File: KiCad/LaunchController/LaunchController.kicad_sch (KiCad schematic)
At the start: 116 parts, among them J1 DC_IN, J10 CONN_SPEAKER, J11 CONN_EXT_I2C_0, J12 CONN_EXT_GPIO_0, J13 CONN_EXT_SPI_0, J14 CONN_EXT_I2C_1, J15 CONN_EXT_GPIO_1, J16 CONN_EXT_SPI_1, J17 CONN_USB, J18 CONN_EXT_I2C_2, J19 CONN_EXT_GPIO_2, J2 JMP_RUN, J20 CONN_EXT_SPI_2, J21 CONN_EXT_I2C_3, J22 CONN_EXT_GPIO_3, J3 CONN_ICSP, J4 CONN_RS485, J5 JMP_KILL, J6 CONN_AUDIO, J7 L, J8 R, J9 CONN_EXT_UART, P1 USB_C_Plug_USB2.0, Q1 TJ8S06M3L, Q2 TJ8S06M3L, Q3 2SC3325, SW1 SW_RESET, U1 SI-8008HFE, U3 INA219BxDCN, U4 INA219BxDCN, U5 74HC14, U6 LTC485CN8#PBF, U7 FT232RL, U8 ATmega2560-16A, Y1 16MHz

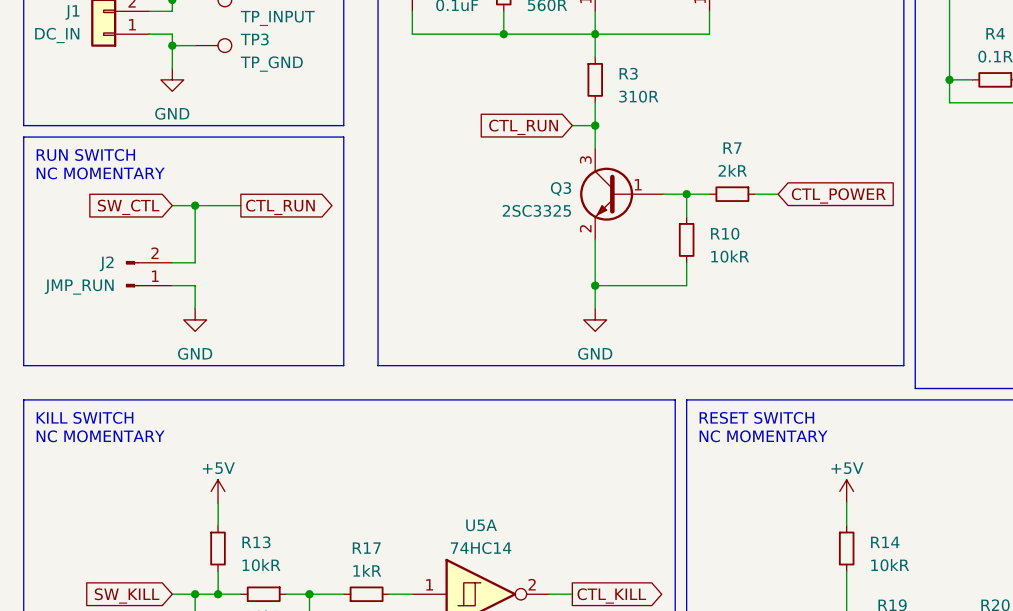
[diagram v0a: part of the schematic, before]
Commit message: スイッチの接点方式を修正
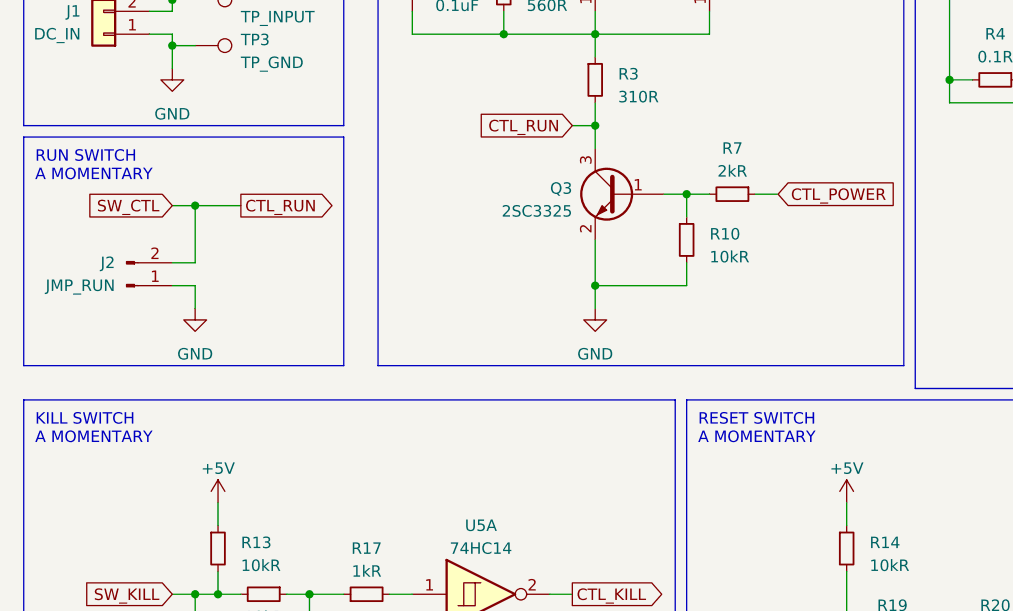
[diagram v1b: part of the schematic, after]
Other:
- note added: "KILL SWITCH A MOMENTARY"
- note added: "RESET SWITCH A MOMENTARY"
- note added: "RUN SWITCH A MOMENTARY"
- note removed: "KILL SWITCH NC MOMENTARY"
- note removed: "RESET SWITCH NC MOMENTARY"
- note removed: "RUN SWITCH NC MOMENTARY"
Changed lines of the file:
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@@
     (fill (type none))
   )
-  (text "RESET SWITCH\nNC MOMENTARY" (at 87.63 82.55 0)
+  (text "RESET SWITCH\nA MOMENTARY" (at 87.63 82.55 0)
     (effects (font (size 1.27 1.27)) (justify left bottom))
   )
@@
     (effects (font (size 1.27 1.27)) (justify left bottom))
   )
-  (text "RUN SWITCH\nNC MOMENTARY" (at 13.97 53.34 0)
+  (text "RUN SWITCH\nA MOMENTARY" (at 13.97 53.34 0)
     (effects (font (size 1.27 1.27)) (justify left bottom))
   )
@@
     (effects (font (size 1.27 1.27)) (justify left bottom))
   )
-  (text "KILL SWITCH\nNC MOMENTARY" (at 13.97 82.55 0)
+  (text "KILL SWITCH\nA MOMENTARY" (at 13.97 82.55 0)
     (effects (font (size 1.27 1.27)) (justify left bottom))
   )

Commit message: 一通り部品を選定
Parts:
- removed D5: D_Schottky_Small, symbol Device:D_Schottky_Small
- removed P1: USB_C_Plug_USB2.0, symbol Connector:USB_C_Plug_USB2.0
- removed R2: 5kR, symbol Device:R_Variable
- added D5: GS1010FL, Diode_SMD:D_SOD-123F, symbol Device:D_Small
- added J20: USB_B_Micro, Connector_USB:USB_Micro-B_Wuerth_629105150521, symbol Connector:USB_B_Micro
- added RV1: 5kR, Potentiometer_THT:Potentiometer_Bourns_3296W_Vertical, symbol Device:R_Potentiometer_Small
- C1, C6: footprint (none) -> Capacitor_THT:CP_Radial_D12.5mm_P5.00mm
- C10, C11, C12, C13, C14, C15, C16, C17, C18, C19, C2, C20, C21, C22, C23, C3, C4, C5, C7, C8, C9: footprint (none) -> Capacitor_SMD:C_0603_1608Metric_Pad1.08x0.95mm_HandSolder
- D1: footprint (none) -> Diode_SMD:D_SOD-123F
- D2, D4: value D_Small -> GS1010FL; footprint (none) -> Diode_SMD:D_SOD-123F
- D3: footprint (none) -> Package_TO_SOT_THT:TO-220-3_Vertical
- D6, D7: value SM6T200A -> SMAJ45A; footprint Diode_SMD:D_SMB -> Diode_SMD:D_SMA_Handsoldering
- F1: value 500mA -> MF-NSMF050; footprint (none) -> Fuse:Fuse_1206_3216Metric_Pad1.42x1.75mm_HandSolder
- J1, J10: footprint (none) -> Connector_JST:JST_XH_B2B-XH-A_1x02_P2.50mm_Vertical
- J11, J12, J14, J15, J18, J19, J4, J6, J9: footprint (none) -> Connector_JST:JST_XH_B4B-XH-A_1x04_P2.50mm_Vertical
- J13, J16, J17: footprint (none) -> Connector_JST:JST_XH_B6B-XH-A_1x06_P2.50mm_Vertical
- J2, J5: footprint (none) -> Connector_PinHeader_2.54mm:PinHeader_1x02_P2.54mm_Vertical
- J21: renamed from J20; footprint (none) -> Connector_JST:JST_XH_B6B-XH-A_1x06_P2.50mm_Vertical
- J22: renamed from J21; footprint (none) -> Connector_JST:JST_XH_B4B-XH-A_1x04_P2.50mm_Vertical
- J23: renamed from J22; footprint (none) -> Connector_JST:JST_XH_B4B-XH-A_1x04_P2.50mm_Vertical
- J3: footprint (none) -> Connector_PinSocket_2.54mm:PinSocket_1x06_P2.54mm_Vertical
- J7, J8: footprint (none) -> Connector_PinHeader_2.54mm:PinHeader_1x08_P2.54mm_Vertical
- L1: footprint (none) -> Inductor_THT:L_Toroid_Vertical_L26.7mm_W14.0mm_P10.16mm_Pulse_D
- L2: footprint (none) -> Inductor_SMD:L_1210_3225Metric_Pad1.42x2.65mm_HandSolder
- Q3: value 2SC3325 -> 2SC3325-Y; footprint (none) -> Package_TO_SOT_SMD:SC-59_Handsoldering
- R1: value 560R -> 560R1/2W; footprint (none) -> Resistor_SMD:R_1206_3216Metric_Pad1.30x1.75mm_HandSolder
- R10: renamed from R11; footprint (none) -> Resistor_SMD:R_0603_1608Metric_Pad0.98x0.95mm_HandSolder
- R11: renamed from R12; footprint (none) -> Resistor_SMD:R_0603_1608Metric_Pad0.98x0.95mm_HandSolder
- R12: renamed from R13; footprint (none) -> Resistor_SMD:R_0603_1608Metric_Pad0.98x0.95mm_HandSolder
- R13: renamed from R14; footprint (none) -> Resistor_SMD:R_0603_1608Metric_Pad0.98x0.95mm_HandSolder
- R14: renamed from R15; footprint (none) -> Resistor_SMD:R_0603_1608Metric_Pad0.98x0.95mm_HandSolder
- R15: renamed from R16; footprint (none) -> Resistor_SMD:R_0603_1608Metric_Pad0.98x0.95mm_HandSolder
- R16: renamed from R17; footprint (none) -> Resistor_SMD:R_0603_1608Metric_Pad0.98x0.95mm_HandSolder
- R17: renamed from R18; footprint (none) -> Resistor_SMD:R_0603_1608Metric_Pad0.98x0.95mm_HandSolder
- R18: renamed from R19; footprint (none) -> Resistor_SMD:R_0603_1608Metric_Pad0.98x0.95mm_HandSolder
- R19: renamed from R20; footprint (none) -> Resistor_SMD:R_0603_1608Metric_Pad0.98x0.95mm_HandSolder
- R2: renamed from R3; value 310R -> 330R1/2W; footprint (none) -> Resistor_SMD:R_1206_3216Metric_Pad1.30x1.75mm_HandSolder
- R20: renamed from R21; footprint (none) -> Resistor_SMD:R_0603_1608Metric_Pad0.98x0.95mm_HandSolder
- R21: renamed from R22; footprint (none) -> Resistor_SMD:R_0603_1608Metric_Pad0.98x0.95mm_HandSolder
- R22: renamed from R23; footprint (none) -> Resistor_SMD:R_0603_1608Metric_Pad0.98x0.95mm_HandSolder
- R23: renamed from R24; footprint (none) -> Resistor_SMD:R_0603_1608Metric_Pad0.98x0.95mm_HandSolder
- R24: renamed from R25; footprint (none) -> Resistor_SMD:R_0603_1608Metric_Pad0.98x0.95mm_HandSolder
- R25: renamed from R26; footprint (none) -> Resistor_SMD:R_0603_1608Metric_Pad0.98x0.95mm_HandSolder
- R26: renamed from R27; footprint (none) -> Resistor_SMD:R_0603_1608Metric_Pad0.98x0.95mm_HandSolder
- R27: renamed from R28; footprint (none) -> Resistor_SMD:R_0603_1608Metric_Pad0.98x0.95mm_HandSolder
- R28: renamed from R29; footprint (none) -> Resistor_SMD:R_0603_1608Metric_Pad0.98x0.95mm_HandSolder
- R29: renamed from R30; footprint (none) -> Resistor_SMD:R_0603_1608Metric_Pad0.98x0.95mm_HandSolder
- R3: renamed from R4; value 0.1R -> 0.1R2W; footprint (none) -> Resistor_SMD:R_2816_7142Metric_Pad3.20x4.45mm_HandSolder
- R30: renamed from R31; footprint (none) -> Resistor_SMD:R_0603_1608Metric_Pad0.98x0.95mm_HandSolder
- R31: renamed from R32; footprint (none) -> Resistor_SMD:R_0603_1608Metric_Pad0.98x0.95mm_HandSolder
- R4: renamed from R5; value 0.1R -> 0.1R2W; footprint (none) -> Resistor_SMD:R_2816_7142Metric_Pad3.20x4.45mm_HandSolder
- R5: renamed from R6; footprint (none) -> Resistor_SMD:R_0603_1608Metric_Pad0.98x0.95mm_HandSolder
- R6: renamed from R7; footprint (none) -> Resistor_SMD:R_0603_1608Metric_Pad0.98x0.95mm_HandSolder
- R7: renamed from R8; footprint (none) -> Resistor_SMD:R_0603_1608Metric_Pad0.98x0.95mm_HandSolder
- R8: renamed from R9; footprint (none) -> Resistor_SMD:R_0603_1608Metric_Pad0.98x0.95mm_HandSolder
- R9: renamed from R10; footprint (none) -> Resistor_SMD:R_0603_1608Metric_Pad0.98x0.95mm_HandSolder
- SW1: footprint (none) -> Button_Switch_THT:SW_PUSH_6mm_H7.3mm
- TP1, TP10, TP11, TP12, TP13, TP14, TP15, TP2, TP3, TP4, TP5, TP6, TP7, TP8, TP9: footprint (none) -> TestPoint:TestPoint_THTPad_D2.5mm_Drill1.2mm
- U3, U4: value INA219BxDCN -> INA219BIDCNT
- U5: value 74HC14 -> U74HC14; footprint (none) -> Package_DIP:DIP-14_W7.62mm
- U8: value ATmega2560-16A -> ATMEGA2560-16AUR
- Y1: value 16MHz -> HUSG-16.000-20; footprint Crystal:Crystal_C26-LF_D2.1mm_L6.5mm_Horizontal_1EP_style2 -> Crystal:Crystal_HC49-U_Vertical
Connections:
- net +5V: now also D5.1 (K)
- net CTL_RESET: now also D5.2 (A)
- net GND: now also J20.5 (GND), J20.6 (Shield)
- net USB_D+: now also J20.3 (D+)
- net USB_D-: now also J20.2 (D-)
- net USB_VBUS: now also J20.1 (VBUS)
- net at R5.1, U1.4 (FB): now also RV1.2, RV1.3
- net at C6.1, L1.2, R4.2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: now also RV1.1
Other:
- moved on the sheet: C7, R10, R11, R4, R5, TP1, U4

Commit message: ボード設計中（地獄）
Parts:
- R14: value 10kR -> 120R
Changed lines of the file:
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@@
       (effects (font (size 1.27 1.27)) (justify right))
     )
-    (property "Value" "10kR" (at 381 98.425 0)
+    (property "Value" "120R" (at 381 98.425 0)
       (effects (font (size 1.27 1.27)) (justify right))
     )
@@
       (effects (font (size 1.27 1.27)) hide)
     )
-    (property "Datasheet" "https://www.chip1stop.com/view/dispDetail/DispDetail?partId=ROHM-0021098" (at 378.46 96.52 0)
+    (property "Datasheet" "https://www.chip1stop.com/view/dispDetail/DispDetail?partId=ROHM-0040116" (at 378.46 96.52 0)
       (effects (font (size 1.27 1.27)) hide)
     )

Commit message: 修正を回路図に反映
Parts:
- removed C15, C16, C5: 0.1uF, Capacitor_SMD:C_0603_1608Metric_Pad1.08x0.95mm_HandSolder, symbol Device:C_Small
- removed C2: 1uF, Capacitor_SMD:C_0603_1608Metric_Pad1.08x0.95mm_HandSolder, symbol Device:C_Small
- removed C6: 1000uF, Capacitor_THT:CP_Radial_D12.5mm_P5.00mm, symbol Device:C_Polarized_Small
- removed D1: SS2040FL, Diode_SMD:D_SOD-123F, symbol Device:D_Schottky_Small
- removed D2, D4: GS1010FL, Diode_SMD:D_SOD-123F, symbol Device:D_Small
- removed D3: MBR3045FCT, Package_TO_SOT_THT:TO-220-3_Vertical, symbol Device:D_Schottky_Dual_CommonCathode_AKA_Parallel
- removed J17: CONN_USB, Connector_JST:JST_XH_B6B-XH-A_1x06_P2.50mm_Vertical, symbol Connector_Generic:Conn_01x06
- removed J4: CONN_RS485, Connector_JST:JST_XH_B4B-XH-A_1x04_P2.50mm_Vertical, symbol Connector_Generic:Conn_01x04
- removed J5: JMP_KILL, Connector_PinHeader_2.54mm:PinHeader_1x02_P2.54mm_Vertical, symbol Connector:Conn_01x02_Pin
- removed J6: CONN_AUDIO, Connector_JST:JST_XH_B4B-XH-A_1x04_P2.50mm_Vertical, symbol Connector_Generic:Conn_01x04
- removed L1: 100uH, Inductor_THT:L_Toroid_Vertical_L26.7mm_W14.0mm_P10.16mm_Pulse_D, symbol Device:L
- removed R13, R15, R18: 10kR, Resistor_SMD:R_0603_1608Metric_Pad0.98x0.95mm_HandSolder, symbol Device:R_Small
- removed R16, R19: 1kR, Resistor_SMD:R_0603_1608Metric_Pad0.98x0.95mm_HandSolder, symbol Device:R_Small
- removed R31: 5.1kR, Resistor_SMD:R_0603_1608Metric_Pad0.98x0.95mm_HandSolder, symbol Device:R_Small
- removed RV1: 5kR, Potentiometer_THT:Potentiometer_Bourns_3296W_Vertical, symbol Device:R_Potentiometer_Small
- removed U1: SI-8008HFE, Package_TO_SOT_THT:TO-220-5_Vertical, symbol Regulator_Switching:GL2576-ATB5T
- removed U5: U74HC14, Package_DIP:DIP-14_W7.62mm, symbol 74xx:74HC14
- added D2, D4: SS2040FL, Diode_SMD:D_SOD-123F, symbol Device:D_Schottky_Small
- added D28: GS1010FL, Diode_SMD:D_SOD-123F, symbol Device:D_Small
- added J17: RJ45, symbol Connector:RJ45
- added J37: VSW_OUT, Connector_JST:JST_XH_B2B-XH-A_1x02_P2.50mm_Vertical, symbol Connector_Generic:Conn_01x02
- added J38: 12V_IN, Connector_JST:JST_XH_B2B-XH-A_1x02_P2.50mm_Vertical, symbol Connector_Generic:Conn_01x02
- added J4: CONN_AUDIO, Connector_JST:JST_XH_B2B-XH-A_1x02_P2.50mm_Vertical, symbol Connector_Generic:Conn_01x02
- added J5: CONN_USB, Connector_JST:JST_XH_B4B-XH-A_1x04_P2.50mm_Vertical, symbol Connector_Generic:Conn_01x04
- added R124, R126: 2kR1/2W, Resistor_SMD:R_0603_1608Metric_Pad0.98x0.95mm_HandSolder, symbol Device:R_Small
- added R125: 12kR1/2W, Resistor_SMD:R_0603_1608Metric_Pad0.98x0.95mm_HandSolder, symbol Device:R_Small
- added R127: 1kR, Resistor_SMD:R_0603_1608Metric_Pad0.98x0.95mm_HandSolder, symbol Device:R_Small
- added TH1: 1kR, symbol Device:Thermistor_NTC
- added U1: 24LC256, symbol Memory_EEPROM:24LC256
- C1: value 1000uF -> 1F; footprint Capacitor_THT:CP_Radial_D12.5mm_P5.00mm -> (none)
- R12: value 10kR -> 1kR
- R5: value 150R -> 12kR1/2W
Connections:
- net +12V: now also D28.1 (K)
- net +5V: now also C1.1, D2.1 (K), TH1.1, U1.8 (VCC); no longer R12.1
- net GND: now also D4.1 (K), J17.1, J17.2, J17.3, J17.6, J17.7, J17.8, J37.1 (Pin_1), J38.1 (Pin_1), J4.1 (Pin_1), J5.1 (Pin_1), R124.1, R126.1, R127.1, U1.1 (A0), U1.2 (A1), U1.3 (A2), U1.4 (GND), U1.7 (WP); no longer J20.6 (Shield), R5.2
- net I2C_SCL: now also U1.6 (SCL)
- net I2C_SDA: now also U1.5 (SDA)
- net UART2_RX: now also R12.1; no longer U8.12 (PH0)
- net USB_D+: now also J5.2 (Pin_2)
- net USB_D-: now also J5.3 (Pin_3)
- net USB_VBUS: now also J5.4 (Pin_4)
- net VREF_VSW: now reaches R5.1
- net VREF_VSW: now also R124.2
- net at R14.1, TP6.1, U6.7 (B): now also J17.5
- net at R14.2, TP5.1, U6.6 (A): now also J17.4
- net at C10.1, C11.1, C8.1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: now also D4.2 (A)
- net at R3.1, U3.2 (IN-): now also R5.2, J37.2 (Pin_2); no longer C1.1
- net at R4.2, U4.1 (IN+): now also J38.2 (Pin_2), R125.2
- net at C10.2, C11.2, U?.3 (OUT): now also D2.2 (A), D28.2 (A)
- net at J7.5 (Pin_5): now also J4.2 (Pin_2)
- net SW_KILL: no longer names the net of R12.2
- net SW_KILL: now also U8.12 (PH0)
- new net USB_SHIELD: J20.6 (Shield)
- new net VREF_12V: R125.1, R126.2
- new net VREF_THERMISTOR: R127.2, TH1.2
- no-connect marks 19 -> 20
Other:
- note added: "EEPROM"
- note removed: "DC/DC CONVERTER 12V"
- note removed: "KILL SWITCH A MOMENTARY"
- note removed: "RESET SWITCH A MOMENTARY"
- moved on the sheet: C10, C11, C19, C21, C23, C7, C8, C9, D6, D7, F1, J20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

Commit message: フィードバックLEDを追加
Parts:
- removed J2: JMP_RUN, Connector_PinHeader_2.54mm:PinHeader_1x02_P2.54mm_Vertical, symbol Connector:Conn_01x02_Pin
- renumbered C3 to C1, C17 to C10, C13 to C11, C14 to C12, C1 to C13, C7 to C14, C8 to C15, C9 to C16, C10 to C17, C11 to C18, C21 to C2, C19 to C3, C23 to C4, C4 to C5, C18 to C6, C20 to C7, C22 to C8, C12 to C9, D6 to D1, D7 to D2, D5 to D3, D28 to D4, D4 to D5, D2 to D6, J18 to J10, J22 to J11, J13 to J12, J16 to J13, J21 to J14, J4 to J15, J10 to J16, J12 to J17, J15 to J18, J5 to J2, J23 to J20, J17 to J21, J7 to J22, J8 to J23, J20 to J3, J37 to J4, J38 to J5, J3 to J6, J9 to J7, J11 to J8, J14 to J9, L2 to L1, Q3 to Q2, Q2 to Q3, R21 to R1, R8 to R10, R5 to R11, R124 to R12, R17 to R13, R20 to R14, R12 to R15, R125 to R16, R126 to R17, R28 to R18, R29 to R19, R22 to R2, R24 to R20, R4 to R21, R25 to R22, R10 to R23, R11 to R24, R26 to R25, R27 to R26, R30 to R27, R14 to R28, R127 to R29, R1 to R3, R2 to R4, R9 to R5, R3 to R7, R23 to R8, R7 to R9, TP2 to TP1, TP13 to TP10, TP14 to TP11, TP15 to TP12, TP5 to TP13, TP6 to TP14, TP4 to TP15, TP3 to TP2, TP7 to TP3, TP8 to TP4, TP9 to TP5, TP10 to TP6, TP11 to TP7, TP1 to TP8, TP12 to TP9, U7 to U1, U1 to U2, U8 to U4, U4 to U5, U6 to U7
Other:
- note removed: "RUN SWITCH A MOMENTARY"
- moved on the sheet: C2, C3, C4, D1, D2, F1, J2, J3, R1, R2, R8, TP3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

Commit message: シートを分割
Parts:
- removed C1, C14, C16, C18, C5: 0.1uF, Capacitor_SMD:C_0603_1608Metric_Pad1.08x0.95mm_HandSolder, symbol Device:C_Small
- removed C15, C17: 10uF, Capacitor_SMD:C_0603_1608Metric_Pad1.08x0.95mm_HandSolder, symbol Device:C_Small
- removed D4: GS1010FL, Diode_SMD:D_SOD-123F, symbol Device:D_Small
- removed D5, D6: SS2040FL, Diode_SMD:D_SOD-123F, symbol Device:D_Schottky_Small
- removed J1: DC_IN, Connector_JST:JST_XH_B2B-XH-A_1x02_P2.50mm_Vertical, symbol Connector_Generic:Conn_01x02
- removed J4: VSW_OUT, Connector_JST:JST_XH_B2B-XH-A_1x02_P2.50mm_Vertical, symbol Connector_Generic:Conn_01x02
- removed J5: 12V_IN, Connector_JST:JST_XH_B2B-XH-A_1x02_P2.50mm_Vertical, symbol Connector_Generic:Conn_01x02
- removed Q1, Q3: TJ8S06M3L, Package_TO_SOT_SMD:TO-252-2, symbol Transistor_FET:QM6015D
- removed Q2: 2SC3325-Y, Package_TO_SOT_SMD:SC-59_Handsoldering, symbol Device:Q_NPN_BEC
- removed R10, R23, R24, R5, R9: 10kR, Resistor_SMD:R_0603_1608Metric_Pad0.98x0.95mm_HandSolder, symbol Device:R_Small
- removed R11, R16: 12kR1/2W, Resistor_SMD:R_0603_1608Metric_Pad0.98x0.95mm_HandSolder, symbol Device:R_Small
- removed R12, R17: 2kR1/2W, Resistor_SMD:R_0603_1608Metric_Pad0.98x0.95mm_HandSolder, symbol Device:R_Small
- removed R21, R7: 0.1R2W, Resistor_SMD:R_2816_7142Metric_Pad3.20x4.45mm_HandSolder, symbol Device:R_Small
- removed R29: 1kR, Resistor_SMD:R_0603_1608Metric_Pad0.98x0.95mm_HandSolder, symbol Device:R_Small
- removed R3: 560R1/2W, Resistor_SMD:R_1206_3216Metric_Pad1.30x1.75mm_HandSolder, symbol Device:R_Small
- removed R4: 330R1/2W, Resistor_SMD:R_1206_3216Metric_Pad1.30x1.75mm_HandSolder, symbol Device:R_Small
- removed R6: 2kR, Resistor_SMD:R_0603_1608Metric_Pad0.98x0.95mm_HandSolder, symbol Device:R_Small
- removed TH1: 1kR, symbol Device:Thermistor_NTC
- removed TP1: TP_INPUT, TestPoint:TestPoint_THTPad_D2.5mm_Drill1.2mm, symbol Connector:TestPoint
- removed TP15: TP_5V, TestPoint:TestPoint_THTPad_D2.5mm_Drill1.2mm, symbol Connector:TestPoint
- removed TP2: TP_GND, TestPoint:TestPoint_THTPad_D2.5mm_Drill1.2mm, symbol Connector:TestPoint
- removed TP8: TP_12V, TestPoint:TestPoint_THTPad_D2.5mm_Drill1.2mm, symbol Connector:TestPoint
- removed U3, U5: INA219BIDCNT, Package_TO_SOT_SMD:SOT-23-8, symbol Sensor_Energy:INA219BxDCN
- removed U?: NJM7805SDL1, Package_TO_SOT_SMD:TO-252-2, symbol Regulator_Linear:L7812
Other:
- removed sheet Interface
- added sheet Indicator (Indicator.kicad_sch)
- added sheet Power (Power.kicad_sch)
- added sheet Switch (Switch.kicad_sch)
- note removed: "DC/DC CONVERTER 5V"
- note removed: "LOAD SWITCH"
- note removed: "POWER INPUT DC JACK 15-24V"
- note removed: "POWER MONITOR"
- moved on the sheet: C10, C11, C12, C13, C2, C3, C4, C6, C7, C8, C9, D1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

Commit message: 電圧から抵抗値を修正
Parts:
- C13: footprint (none) -> Capacitor_THT:DX_5R5VxxxxU_D19.0mm_P5.00mm
- J21: footprint (none) -> Connector_RJ:RJ45_Wuerth_7499010001A_Horizontal
- U2: footprint (none) -> Package_DIP:DIP-8_W7.62mm
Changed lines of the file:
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@@
       (effects (font (size 1.27 1.27)) (justify left))
     )
-    (property "Footprint" "" (at 199.39 93.98 0)
-      (effects (font (size 1.27 1.27)) hide)
-    )
-    (property "Datasheet" "~" (at 199.39 93.98 0)
+    (property "Footprint" "Capacitor_THT:DX_5R5VxxxxU_D19.0mm_P5.00mm" (at 199.39 93.98 0)
+      (effects (font (size 1.27 1.27)) hide)
+    )
+    (property "Datasheet" "https://akizukidenshi.com/catalog/g/gP-04249/" (at 199.39 93.98 0)
       (effects (font (size 1.27 1.27)) hide)
     )
@@
       (effects (font (size 1.27 1.27)) (justify right))
     )
-    (property "Footprint" "" (at 392.43 31.115 90)
-      (effects (font (size 1.27 1.27)) hide)
-    )
-    (property "Datasheet" "~" (at 392.43 31.115 90)
+    (property "Footprint" "Connector_RJ:RJ45_Wuerth_7499010001A_Horizontal" (at 392.43 31.115 90)
+      (effects (font (size 1.27 1.27)) hide)
+    )
+    (property "Datasheet" "https://www.monotaro.com/g/04423212" (at 392.43 31.115 90)
       (effects (font (size 1.27 1.27)) hide)
     )
@@
       (effects (font (size 1.27 1.27)) (justify left))
     )
-    (property "Footprint" "" (at 223.52 29.21 0)
-      (effects (font (size 1.27 1.27)) hide)
-    )
-    (property "Datasheet" "http://ww1.microchip.com/downloads/en/devicedoc/21203m.pdf" (at 223.52 29.21 0)
-      (effects (font (size 1.27 1.27)) hide)
-    )
+    (property "Footprint" "Package_DIP:DIP-8_W7.62mm" (at 223.52 29.21 0)
+      (effects (font (size 1.27 1.27)) hide)
+    )
+    (property "Datasheet" "https://akizukidenshi.com/catalog/g/gI-00705/" (at 223.52 29.21 0)
+      (effects (font (size 1.27 1.27)) hide)
+    )

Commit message: さらに分割
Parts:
- removed J10: CONN_EXT_I2C_2, Connector_JST:JST_XH_B4B-XH-A_1x04_P2.50mm_Vertical, symbol Connector_Generic:Conn_01x04
- removed J11: CONN_EXT_I2C_3, Connector_JST:JST_XH_B4B-XH-A_1x04_P2.50mm_Vertical, symbol Connector_Generic:Conn_01x04
- removed J12: CONN_EXT_SPI_0, Connector_JST:JST_XH_B6B-XH-A_1x06_P2.50mm_Vertical, symbol Connector_Generic:Conn_01x06
- removed J13: CONN_EXT_SPI_1, Connector_JST:JST_XH_B6B-XH-A_1x06_P2.50mm_Vertical, symbol Connector_Generic:Conn_01x06
- removed J14: CONN_EXT_SPI_2, Connector_JST:JST_XH_B6B-XH-A_1x06_P2.50mm_Vertical, symbol Connector_Generic:Conn_01x06
- removed J15: CONN_AUDIO, Connector_JST:JST_XH_B2B-XH-A_1x02_P2.50mm_Vertical, symbol Connector_Generic:Conn_01x02
- removed J16: CONN_SPEAKER, Connector_JST:JST_XH_B2B-XH-A_1x02_P2.50mm_Vertical, symbol Connector_Generic:Conn_01x02
- removed J17: CONN_EXT_GPIO_0, Connector_JST:JST_XH_B4B-XH-A_1x04_P2.50mm_Vertical, symbol Connector_Generic:Conn_01x04
- removed J18: CONN_EXT_GPIO_1, Connector_JST:JST_XH_B4B-XH-A_1x04_P2.50mm_Vertical, symbol Connector_Generic:Conn_01x04
- removed J19: CONN_EXT_GPIO_2, Connector_JST:JST_XH_B4B-XH-A_1x04_P2.50mm_Vertical, symbol Connector_Generic:Conn_01x04
- removed J20: CONN_EXT_GPIO_3, Connector_JST:JST_XH_B4B-XH-A_1x04_P2.50mm_Vertical, symbol Connector_Generic:Conn_01x04
- removed J21: RJ45, Connector_RJ:RJ45_Wuerth_7499010001A_Horizontal, symbol Connector:RJ45
- removed J22: L, Connector_PinHeader_2.54mm:PinHeader_1x08_P2.54mm_Vertical, symbol Connector:Conn_01x08_Socket
- removed J23: R, Connector_PinHeader_2.54mm:PinHeader_1x08_P2.54mm_Vertical, symbol Connector:Conn_01x08_Socket
- removed J7: CONN_EXT_UART, Connector_JST:JST_XH_B4B-XH-A_1x04_P2.50mm_Vertical, symbol Connector_Generic:Conn_01x04
- removed J8: CONN_EXT_I2C_0, Connector_JST:JST_XH_B4B-XH-A_1x04_P2.50mm_Vertical, symbol Connector_Generic:Conn_01x04
- removed J9: CONN_EXT_I2C_1, Connector_JST:JST_XH_B4B-XH-A_1x04_P2.50mm_Vertical, symbol Connector_Generic:Conn_01x04
- removed R25, R26, R27: 4.7kR, Resistor_SMD:R_0603_1608Metric_Pad0.98x0.95mm_HandSolder, symbol Device:R_Small
- removed R28: 120R, Resistor_SMD:R_0603_1608Metric_Pad0.98x0.95mm_HandSolder, symbol Device:R_Small
- removed TP13: TP_A, TestPoint:TestPoint_THTPad_D2.5mm_Drill1.2mm, symbol Connector:TestPoint
- removed TP14: TP_B, TestPoint:TestPoint_THTPad_D2.5mm_Drill1.2mm, symbol Connector:TestPoint
- removed U2: 24LC256, Package_DIP:DIP-8_W7.62mm, symbol Memory_EEPROM:24LC256
- removed U7: LTC485CN8#PBF, Package_DIP:DIP-8_W7.62mm, symbol Interface_UART:LT1785xN8
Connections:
- no-connect marks 20 -> 12
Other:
- added sheet Extension (Extension.kicad_sch)
- added sheet Peripheral (Peripheral.kicad_sch)
- note removed: "AUDIO"
- note removed: "EEPROM"
- note removed: "EXTENSION GPIO"
- note removed: "EXTENSION I2C"
- note removed: "EXTENSION SPI"
- note removed: "EXTENSION UART"
- note removed: "RS485"
- moved on the sheet: C10, C11, C12, C13, C2, C3, C4, C6, C7, C8, C9, D1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
